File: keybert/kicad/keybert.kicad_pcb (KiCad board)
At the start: 2 copper layers, 148 x 123 mm, 64 parts, among them U0 ProMicro

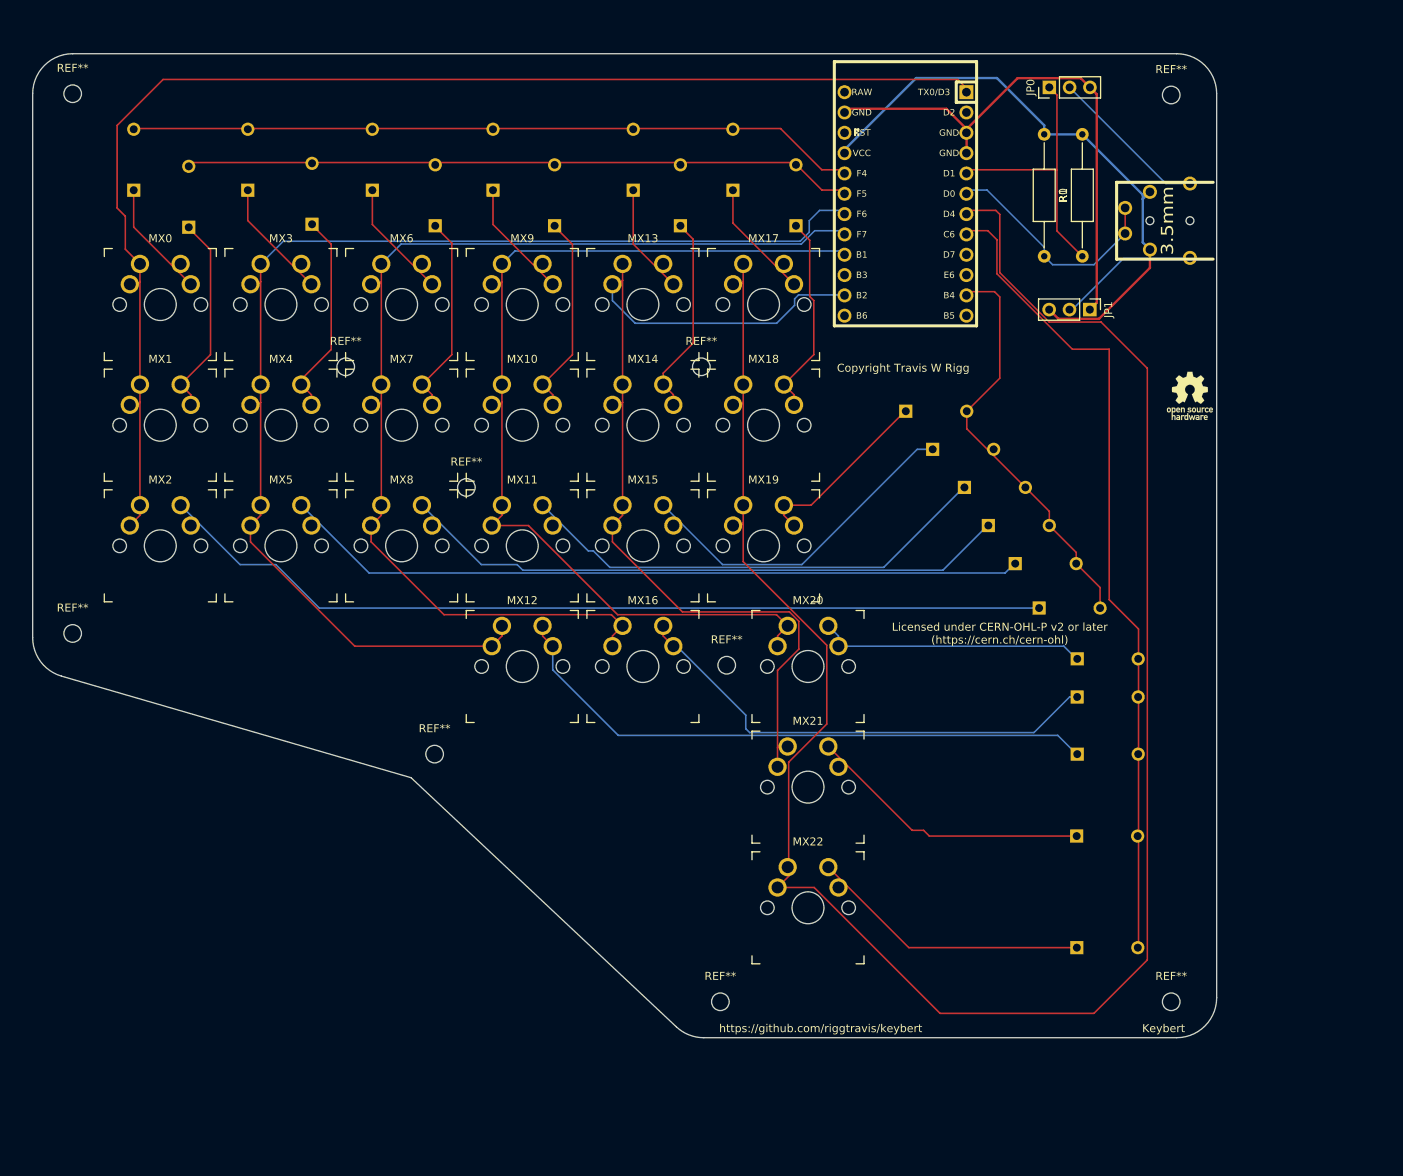
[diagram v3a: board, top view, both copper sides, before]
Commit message: fix: redid PCB due to switch spacing issue
The spacing of the switches was all wrong I discovered upon loading up
the switch plate into FreeCAD. I've redone the basic arrangement of all
electronic parts, but the parts all need, once more to be reconnected.

I also simplified the schematic slightly. I don't like crossed wires
even though the ones that do connect are pretty clear thanks to their
green nodes
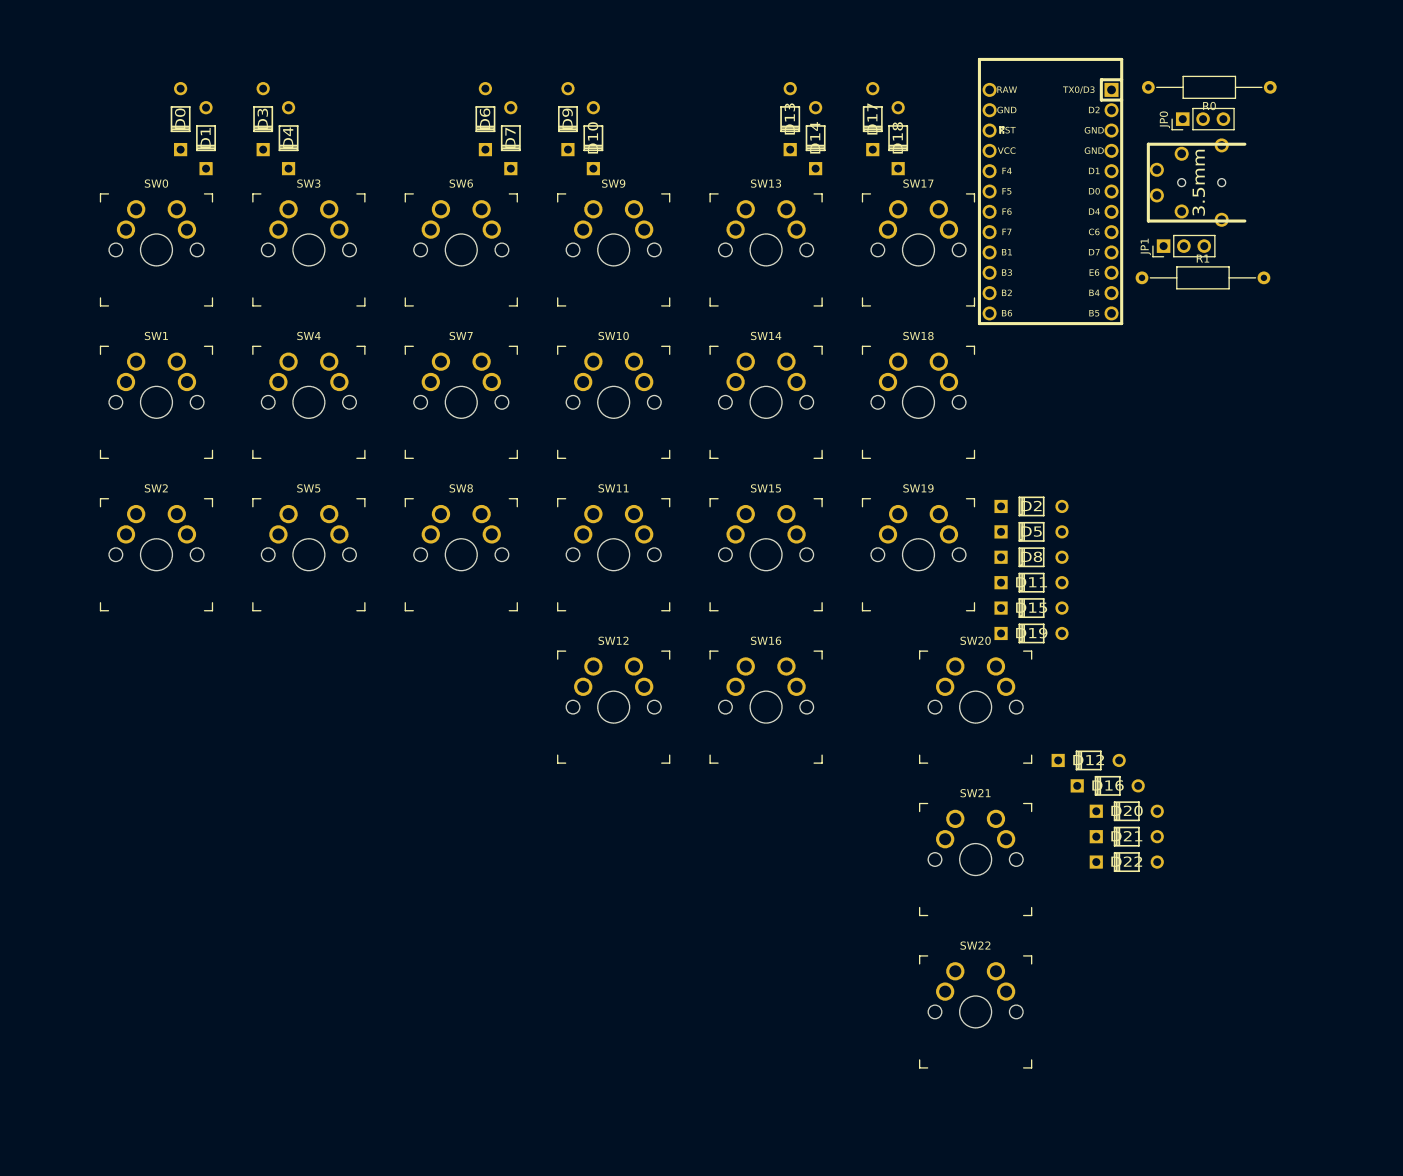
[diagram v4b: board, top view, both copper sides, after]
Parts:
- removed MX0, MX1, MX10, MX11, MX12, MX13, MX14, MX15, MX16, MX17, MX18, MX19, MX2, MX20, MX21, MX22, MX3, MX4, MX5, MX6, MX7, MX8, MX9: MX-NoLED, keyswitches:SW_MX_reversible
- removed REF** (x10): MountingHole_2.2mm_M2, MountingHole:MountingHole_2.2mm_M2
- removed REF** (x2): OSHW-Logo_5.7x6mm_SilkScreen, Symbol:OSHW-Logo_5.7x6mm_SilkScreen
- added SW0: MX-NoLED, keyswitches:SW_MX_reversible, F.Cu at (32.0, 42.5)
- added SW1: MX-NoLED, keyswitches:SW_MX_reversible, F.Cu at (32.0, 61.6)
- added SW10: MX-NoLED, keyswitches:SW_MX_reversible, F.Cu at (89.1, 61.6)
- added SW11: MX-NoLED, keyswitches:SW_MX_reversible, F.Cu at (89.1, 80.6)
- added SW12: MX-NoLED, keyswitches:SW_MX_reversible, F.Cu at (89.1, 99.7)
- added SW13: MX-NoLED, keyswitches:SW_MX_reversible, F.Cu at (108.2, 42.5)
- added SW14: MX-NoLED, keyswitches:SW_MX_reversible, F.Cu at (108.2, 61.6)
- added SW15: MX-NoLED, keyswitches:SW_MX_reversible, F.Cu at (108.2, 80.6)
- added SW16: MX-NoLED, keyswitches:SW_MX_reversible, F.Cu at (108.2, 99.7)
- added SW17: MX-NoLED, keyswitches:SW_MX_reversible, F.Cu at (127.2, 42.5)
- added SW18: MX-NoLED, keyswitches:SW_MX_reversible, F.Cu at (127.2, 61.6)
- added SW19: MX-NoLED, keyswitches:SW_MX_reversible, F.Cu at (127.2, 80.6)
- added SW2: MX-NoLED, keyswitches:SW_MX_reversible, F.Cu at (32.0, 80.6)
- added SW20: MX-NoLED, keyswitches:SW_MX_reversible, F.Cu at (134.4, 99.7)
- added SW21: MX-NoLED, keyswitches:SW_MX_reversible, F.Cu at (134.4, 118.7)
- added SW22: MX-NoLED, keyswitches:SW_MX_reversible, F.Cu at (134.4, 137.8)
- added SW3: MX-NoLED, keyswitches:SW_MX_reversible, F.Cu at (51.0, 42.5)
- added SW4: MX-NoLED, keyswitches:SW_MX_reversible, F.Cu at (51.0, 61.6)
- added SW5: MX-NoLED, keyswitches:SW_MX_reversible, F.Cu at (51.0, 80.6)
- added SW6: MX-NoLED, keyswitches:SW_MX_reversible, F.Cu at (70.1, 42.5)
- added SW7: MX-NoLED, keyswitches:SW_MX_reversible, F.Cu at (70.1, 61.6)
- added SW8: MX-NoLED, keyswitches:SW_MX_reversible, F.Cu at (70.1, 80.6)
- added SW9: MX-NoLED, keyswitches:SW_MX_reversible, F.Cu at (89.1, 42.5)
- D0, D1, D10, D11, D12, D13, D14, D15, D16, D17, D18, D19, D2, D20, D21, D22, D3, D4, D5, D6, D7, D8, D9: moved to F.Cu
- moved D19 30.2 mm to (141.3, 90.5)
- moved R0 28.9 mm to (171.2, 22.2), turned to 180 degrees
- moved D15 21.6 mm to (141.3, 87.3)
- moved D13 20.3 mm to (111.2, 26.2)
- moved D20 19.2 mm to (153.2, 112.7)
- moved D14 18.3 mm to (114.3, 28.6)
- moved D17 18.2 mm to (121.5, 26.2)
- moved U0 18.1 mm to (143.7, 36.5)
- moved JP0 17.1 mm to (160.2, 26.2)
- moved D6 15.0 mm to (73.1, 26.2)
- moved D18 14.6 mm to (124.7, 28.6)
- moved D2 13.6 mm to (141.3, 74.6)
- moved D11 12.8 mm to (141.3, 84.1)
- moved JP1 12.2 mm to (157.8, 42.0), turned to 90 degrees
- moved D7 11.8 mm to (76.2, 28.6)
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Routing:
- net col5: track 253.5 -> 0.00 mm
- net col0: track 163.6 -> 0.00 mm
- net col1: track 153.3 -> 0.00 mm
- net col2: track 136.6 -> 0.00 mm
- net col3: track 124.8 -> 0.00 mm
- net col4: track 120.0 -> 0.00 mm
- net Net-(D2-Pad2): track 112.6 -> 0.00 mm
- net clu0: track 102.8 -> 0.00 mm
- net Net-(D5-Pad2): track 93.1 -> 0.00 mm
- net row0: track 91.0 -> 0.00 mm
- net row1: track 83.6 -> 0.00 mm
- net Net-(D8-Pad2): track 76.4 -> 0.00 mm
- net Net-(D12-Pad2): track 75.9 -> 0.00 mm
- net VCC: track 74.1 -> 0.00 mm
- net GND: track 65.8 -> 0.00 mm
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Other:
- board outline removed
- board text removed: "Copyright Travis W Rigg"
- board text removed: "Keybert"
- board text removed: "Licensed under CERN-OHL-P v2 or later (https://cern.ch/cern-ohl)"
- board text removed: "https://github.com/riggtravis/keybert"

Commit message: feat: remade parametric model of switch plate
I'm going to have a friend help me get it sorted out why the parameters
are coming out so under constrained
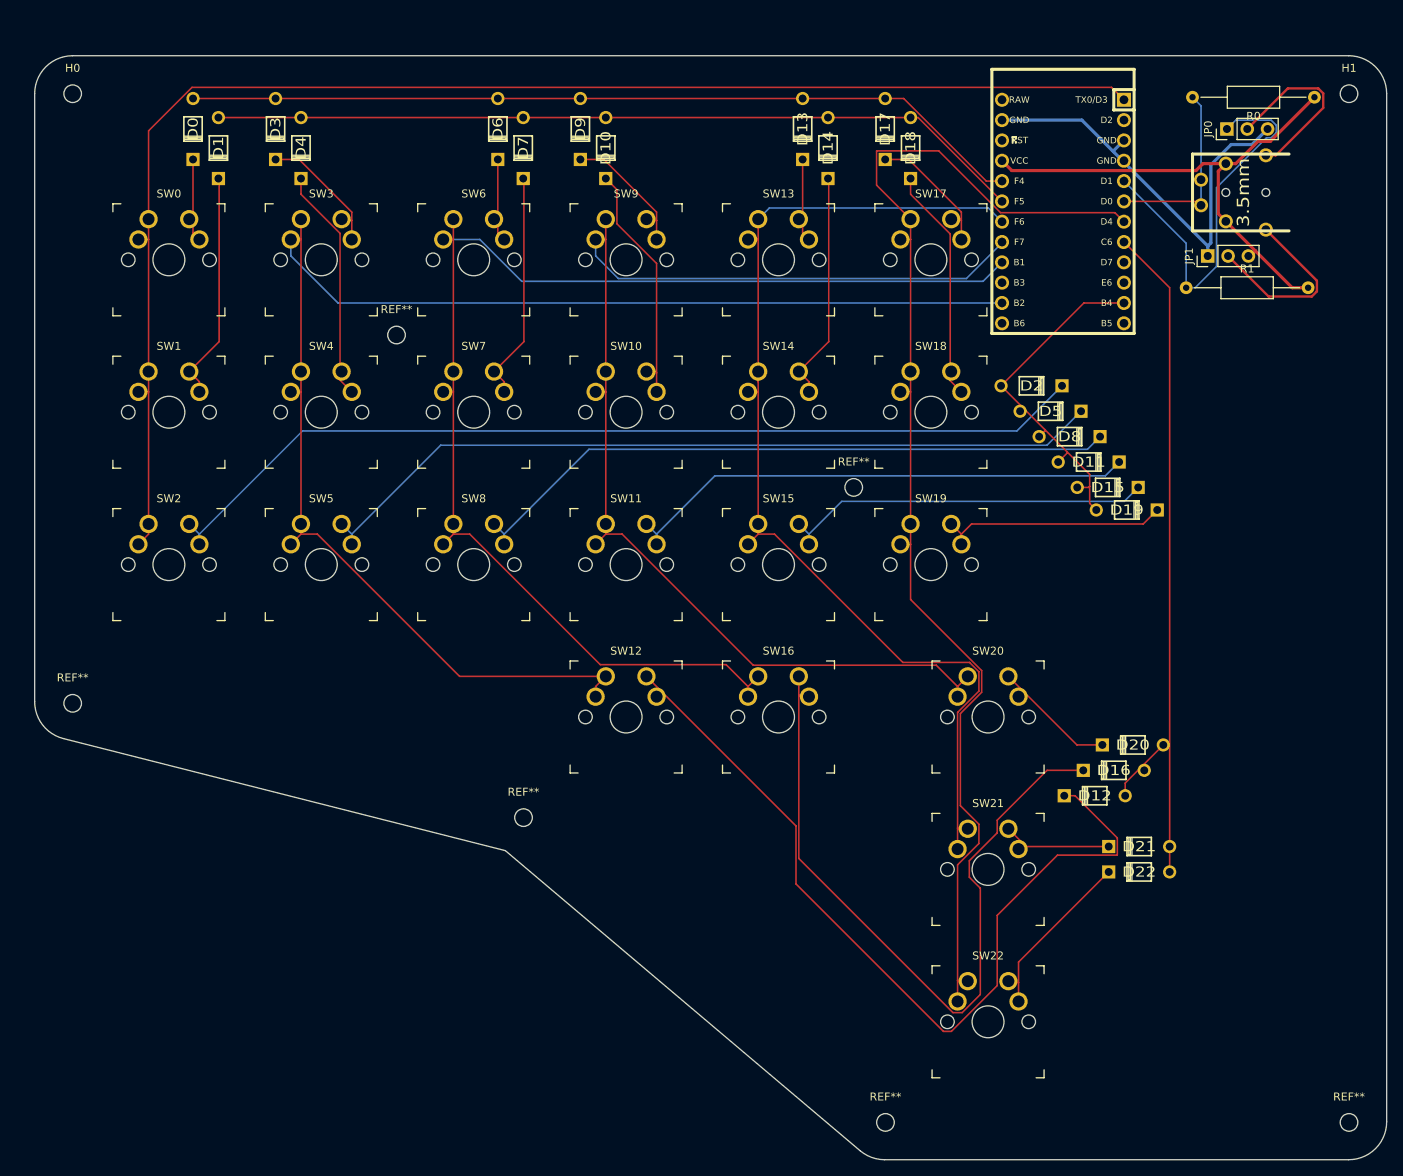
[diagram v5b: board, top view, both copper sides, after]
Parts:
- added H0: MountingHole_2.2mm_M2, MountingHole:MountingHole_2.2mm_M2, F.Cu at (21.5, 23.0)
- added H1: MountingHole_2.2mm_M2, MountingHole:MountingHole_2.2mm_M2, F.Cu at (181.0, 23.0)
- added REF**: MountingHole_2.2mm_M2, MountingHole:MountingHole_2.2mm_M2, F.Cu at (119.1, 72.2)
- added REF**: MountingHole_2.2mm_M2, MountingHole:MountingHole_2.2mm_M2, F.Cu at (62.0, 53.2)
- added REF**: MountingHole_2.2mm_M2, MountingHole:MountingHole_2.2mm_M2, F.Cu at (123.1, 151.6)
- added REF**: MountingHole_2.2mm_M2, MountingHole:MountingHole_2.2mm_M2, F.Cu at (21.5, 99.2)
- added REF**: MountingHole_2.2mm_M2, MountingHole:MountingHole_2.2mm_M2, F.Cu at (181.0, 151.6)
- added REF**: MountingHole_2.2mm_M2, MountingHole:MountingHole_2.2mm_M2, F.Cu at (77.8, 113.5)
- moved D19 19.5 mm to (153.2, 75.0), turned to 0 degrees
- moved D15 17.8 mm to (150.9, 72.2), turned to 0 degrees
- moved D11 16.7 mm to (148.5, 69.0), turned to 0 degrees
- moved D8 15.8 mm to (146.1, 65.9), turned to 0 degrees
- moved D5 15.3 mm to (143.7, 62.7), turned to 0 degrees
- moved D2 15.1 mm to (141.3, 59.5), turned to 0 degrees
- moved D20 8.33 mm to (154.0, 104.4)
- moved JP1 5.66 mm to (163.4, 43.3)
- moved TRRS0 5.66 mm to (165.6, 35.3)
- moved R1 5.66 mm to (160.7, 47.3)
- moved JP0 5.66 mm to (165.8, 27.4)
- moved R0 5.66 mm to (176.7, 23.4)
- moved D12 4.47 mm to (149.2, 110.8)
- moved D16 2.08 mm to (151.6, 107.6)
- moved D10 1.98 mm to (88.1, 29.8)
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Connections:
- net Net-(JP0-Pad2) renamed /FLEX0
- net Net-(JP1-Pad2) renamed /FLEX1
- U0 pad 14: col4 -> col1
- U0 pad 16: col3 -> col2
- U0 pad 17: col2 -> col3
- U0 pad 18: col1 -> col4
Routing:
- net col1: track 0.00 -> 185.6 mm
- net col0: track 0.00 -> 179.6 mm
- net col2: track 0.00 -> 164.5 mm
- net col5: track 0.00 -> 154.6 mm
- net col3: track 0.00 -> 154.6 mm
- net col4: track 0.00 -> 136.0 mm
- net Net-(D2-Pad2): track 0.00 -> 118.6 mm
- net Net-(D12-Pad2): track 0.00 -> 106.7 mm
- net row0: track 0.00 -> 105.4 mm
- net row1: track 0.00 -> 102.3 mm
- net Net-(D5-Pad2): track 0.00 -> 100.6 mm
- net Net-(D16-Pad2): track 0.00 -> 92.9 mm
- net clu0: track 0.00 -> 89.4 mm
- net Net-(D8-Pad2): track 0.00 -> 82.6 mm
- net VCC: track 0.00 -> 66.2 mm
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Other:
- board outline added: 169 x 138 mm
